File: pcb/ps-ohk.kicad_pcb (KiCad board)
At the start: 2 copper layers, 190.5 x 229.6 mm, 91 parts

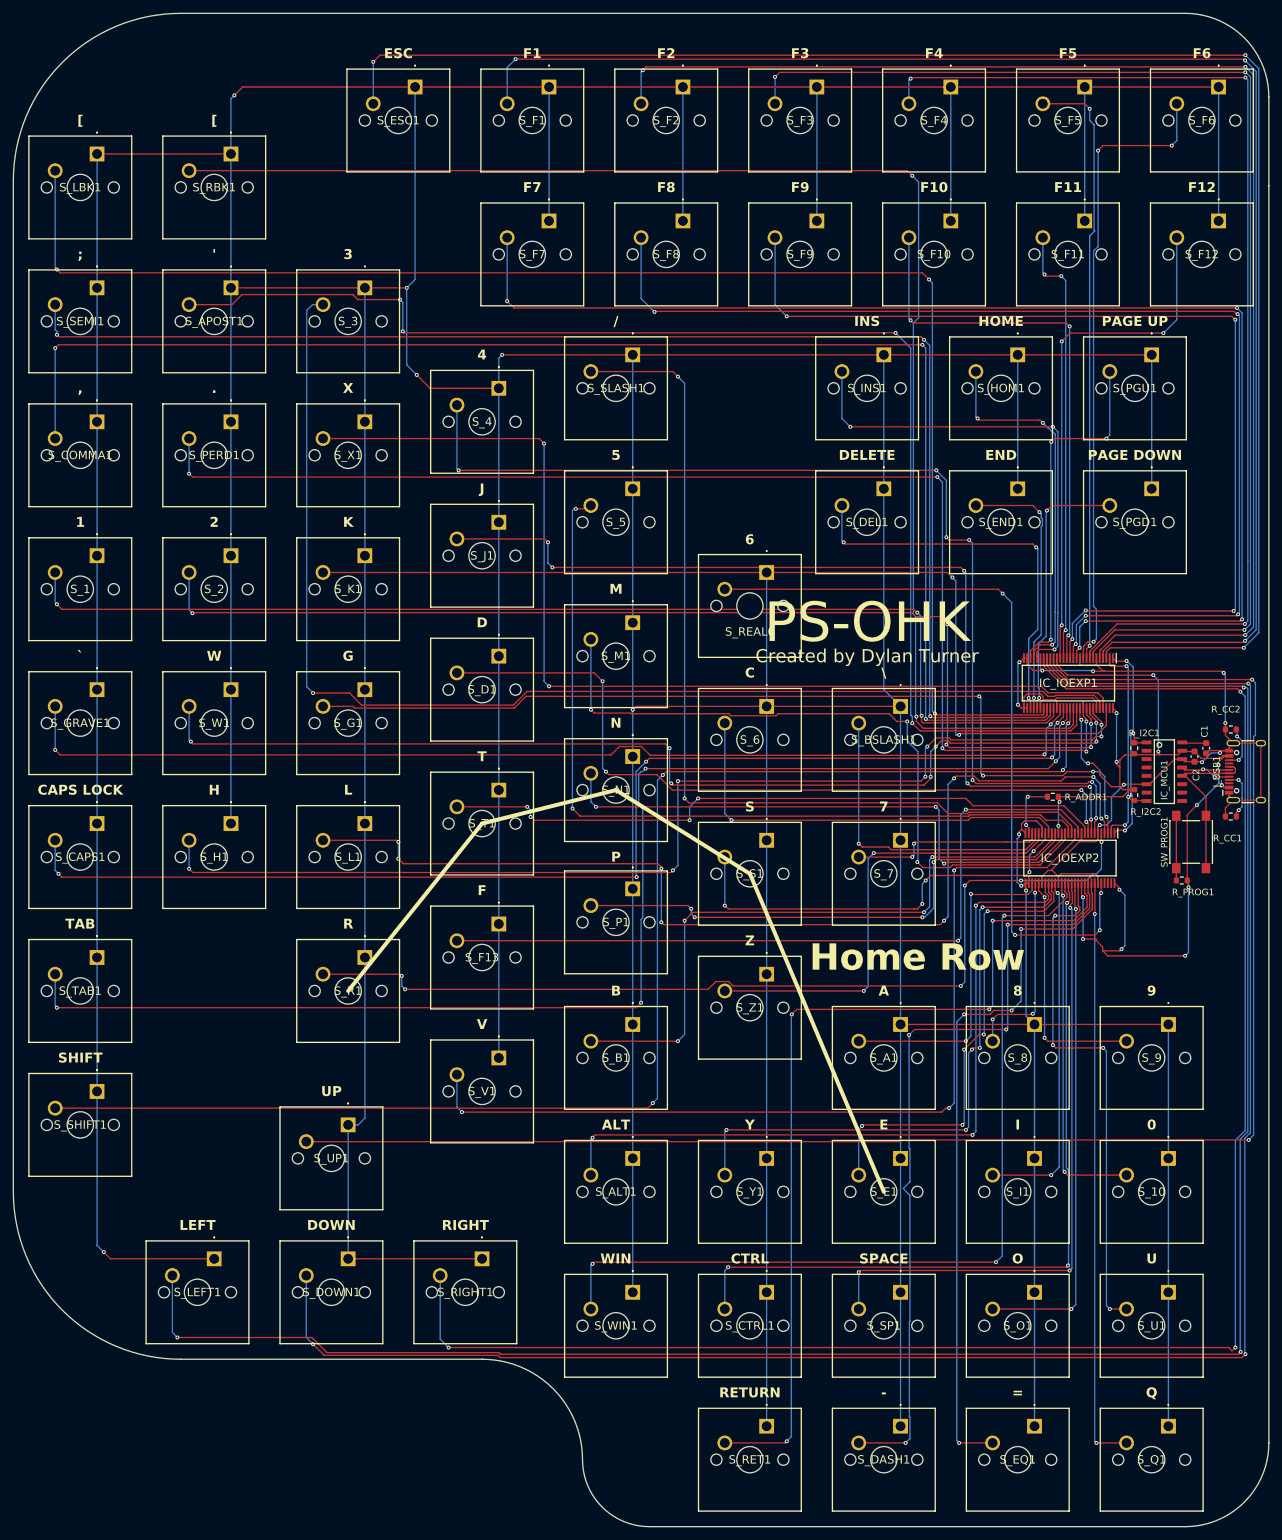
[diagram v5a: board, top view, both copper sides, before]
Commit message: pcb: add backspace and move k
Signed-off-by: Dylan Turner <dylan.turner@tutanota.com>
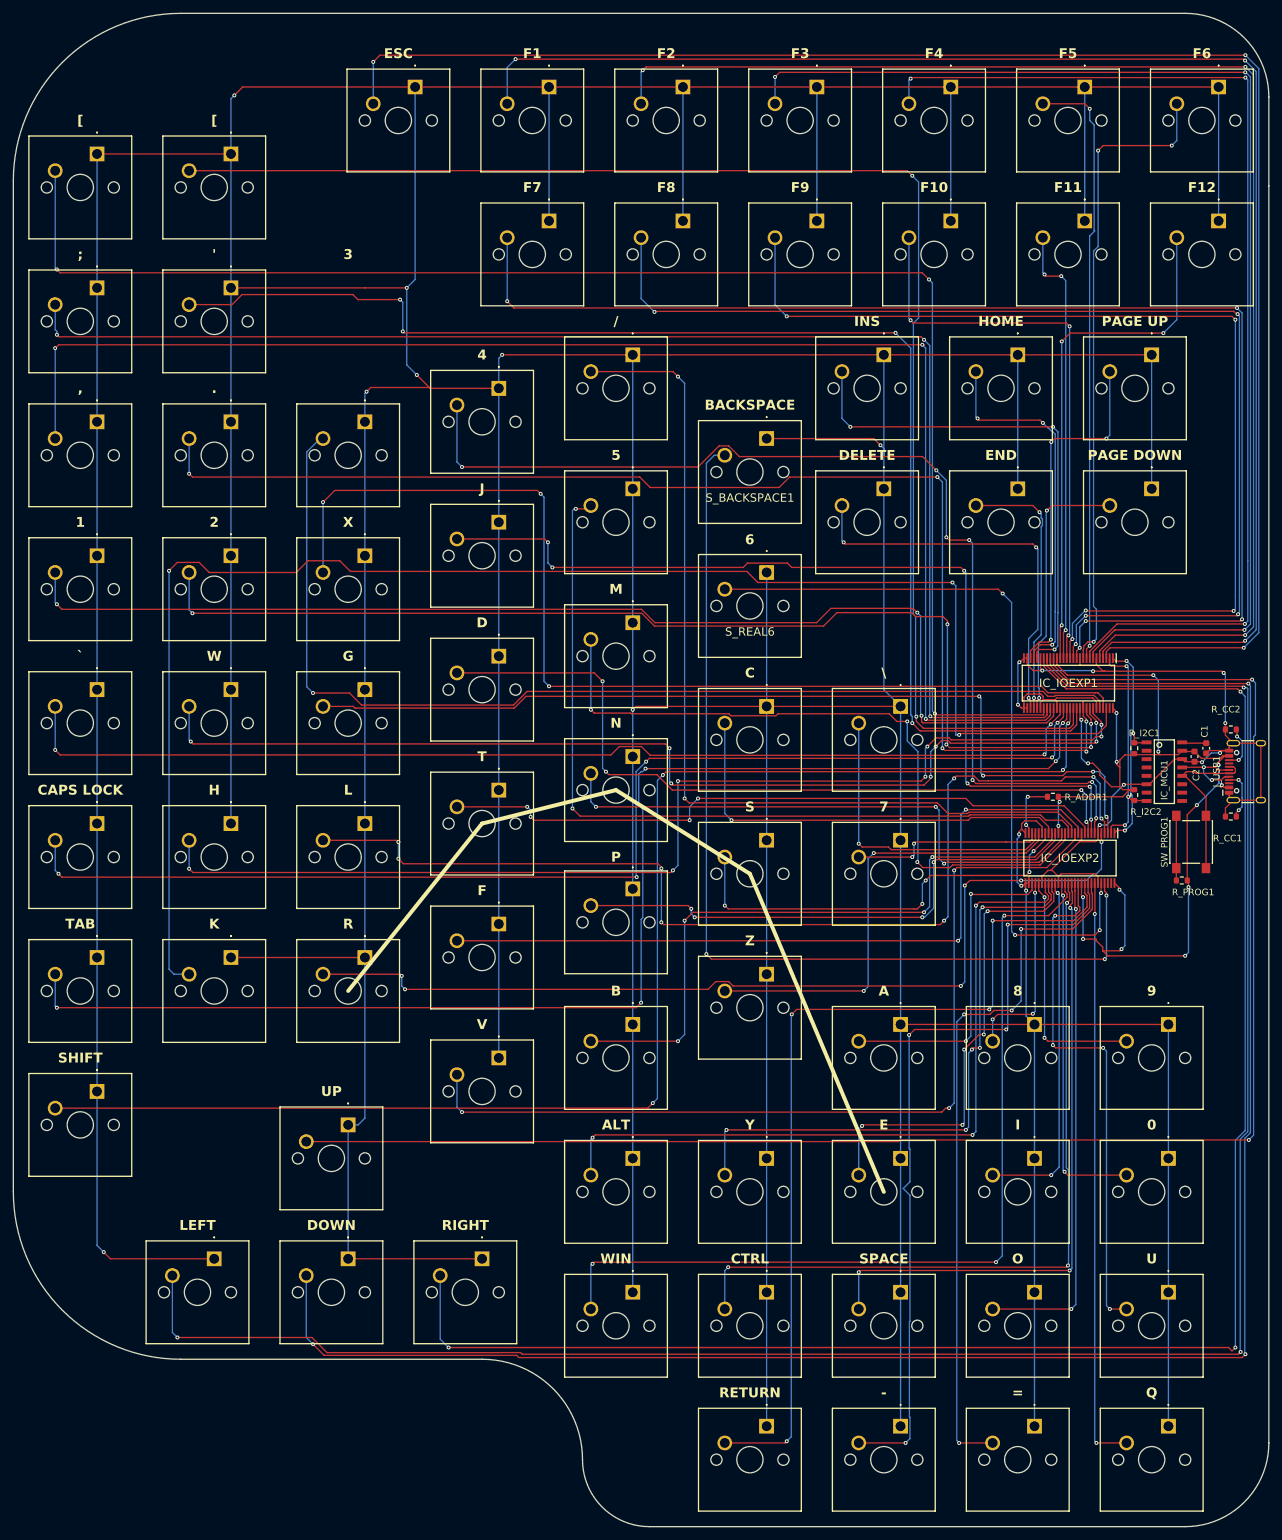
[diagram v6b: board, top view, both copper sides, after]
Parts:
- added S_BACKSPACE1: ~, COM-13834:COM13834, F.Cu at (129.5, 63.5)
- moved S_K1 64.3 mm to (48.3, 142.2)
- moved S_3 20.3 mm to (68.6, 61.0)
- moved S_X1 20.3 mm to (68.6, 81.3)
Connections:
- IC_IOEXP2 pad 53: unconnected-(IC_IOEXP2-IO4_6-Pad53) -> /KEY_BACKSPACE
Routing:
- net /KEY_BACKSPACE: track 0.00 -> 150.3 mm, vias 0 -> 3
- net /KEY_K: track 146.0 -> 235.3 mm, vias 2 -> 3
- net GND: track 1924.8 -> 1958.9 mm, vias 19 -> 21
- net /KEY_3: track 184.0 -> 163.0 mm
- net /KEY_X: track 157.3 -> 160.7 mm, vias 2 -> 3
- net /KEY_4: track 160.7 -> 162.7 mm
- net /KEY_1: track 174.6 -> 176.4 mm
- net /KEY_2: track 168.7 -> 170.5 mm
- net /KEY_PERD: track 191.4 -> 192.7 mm
- net /USB-: track 11.8 -> 12.8 mm
- net /KEY_J: track 139.2 -> 139.7 mm
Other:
- board text added: "BACKSPACE"
- board text added: "r2"
- board text removed: "Home Row"
